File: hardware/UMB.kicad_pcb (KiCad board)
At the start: 6 copper layers, 128.8 x 67 mm, 172 parts, among them J1 PinHeader 02x04, J10 PH1-03-UA, J11 PH1-03-UA, J12 PH1-03-UA, J13 Conn_01x05, J14 Conn_01x05, J15 Conn_01x05, J16 Conn_01x05, J17 Conn_01x05, J18 Conn_01x05, J19 Conn_01x03, J2 PinHeader 02x04, J20 Conn_01x03, J21 Conn_01x03, J22 Conn_01x03, J23 Conn_01x03, J24 Conn_01x03, J25 Conn_01x02, J26 Conn_01x02, J27 FTSH-107-01-L-D-K, J3 PinHeader 02x04, J4 PinHeader 02x04, J5 PinHeader 02x04, J6 PinHeader 02x04, J7 PH1-03-UA, J8 PH1-03-UA, J9 PH1-03-UA, U1 STM32G0C1KCTxN, U10 LDK320ADU120R, U11 INA2128UA_1K, U12 INA2128UA_1K, U13 INA2128UA_1K, U14 TLC274AIDR, U15 TLC274AIDR, U16 TLC274AIDR, U2 ADS114S08BIPBSR, U3 ADM3057ExRW, U4 TPS563300DRLR, U5 TPS563219ADDFR, U6 LM2940SX-12_NOPB, U7 LM1117IMP-5.0, U8 TLV743P, U9 AP2127N3-1.5

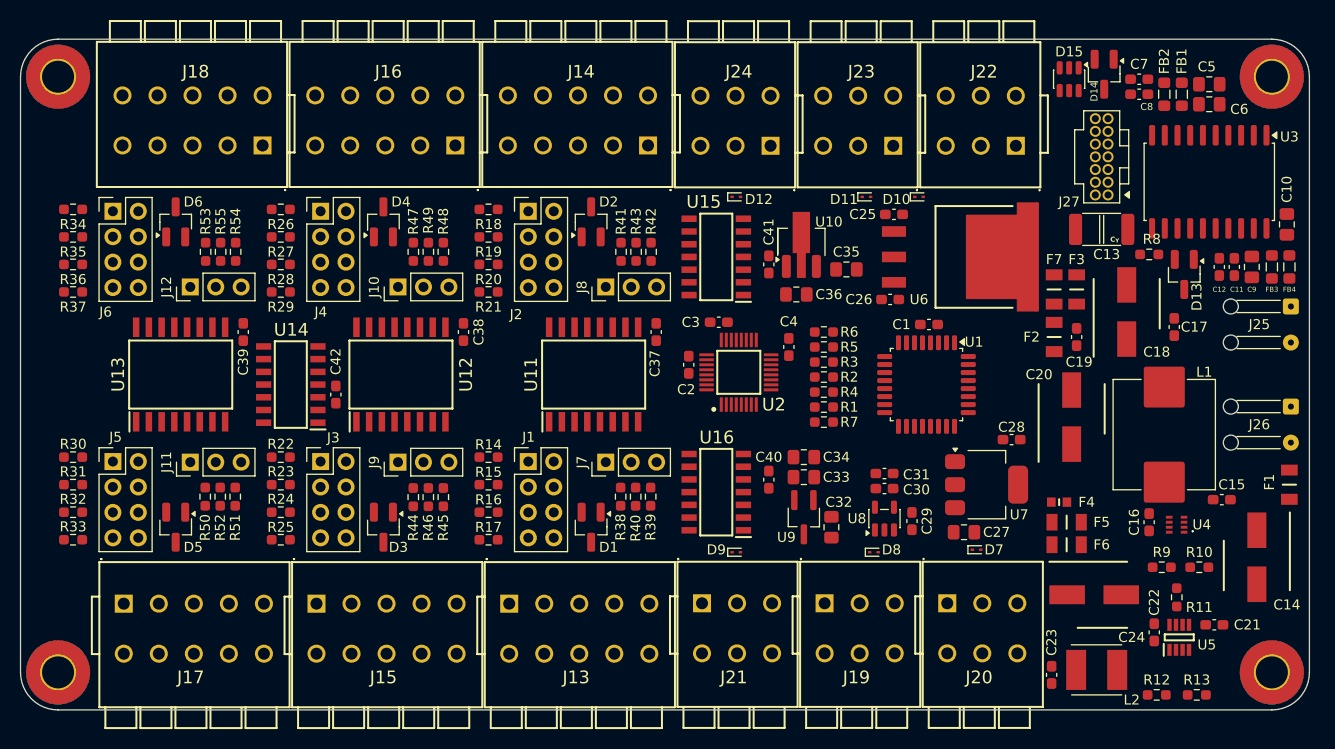
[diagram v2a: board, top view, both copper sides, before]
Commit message: Finished routing on PCB
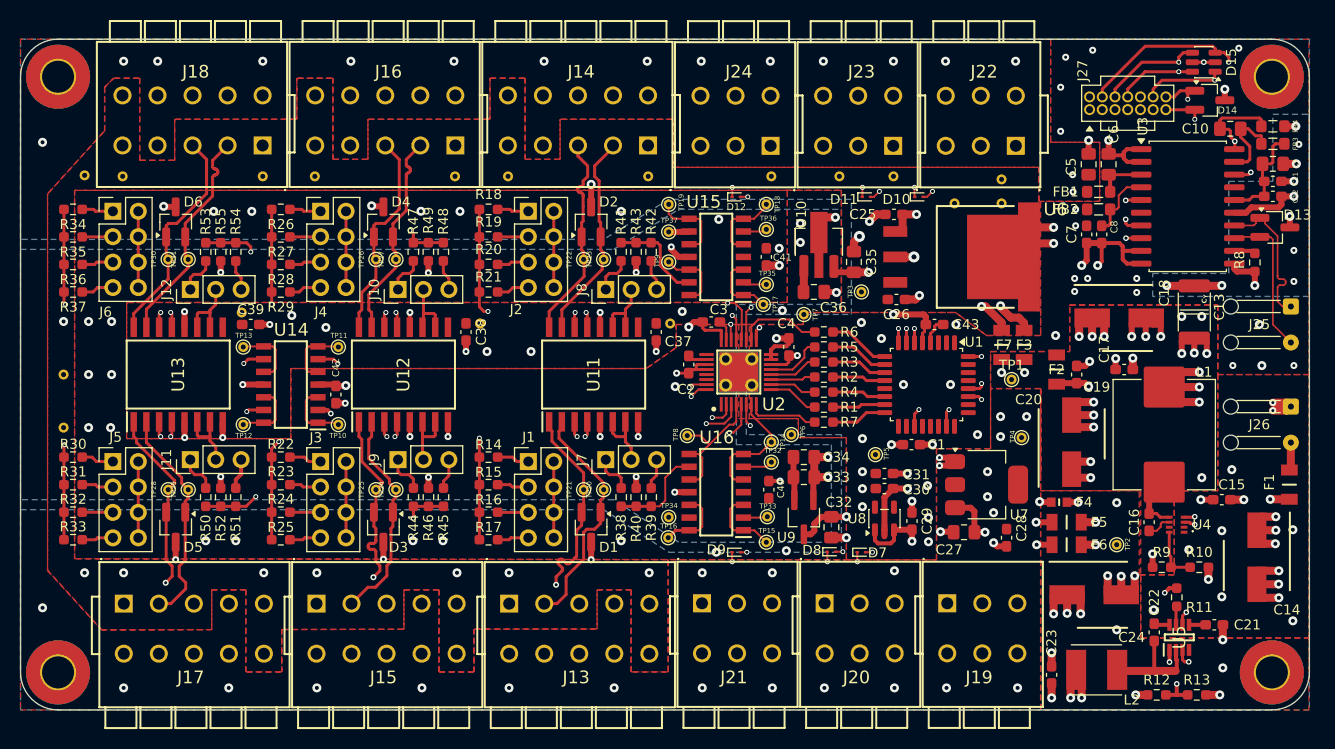
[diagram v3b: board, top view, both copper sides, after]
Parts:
- added ?: , , F.Cu at (74.1, 106.3)
- added ?: , , F.Cu at (150.0, 95.4)
- added ?: , , F.Cu at (56.3, 112.5)
- added ?: , , F.Cu at (114.7, 92.7)
- added ?: , , F.Cu at (133.8, 92.7)
- added ?: , , F.Cu at (145.3, 95.4)
- added ?: , , F.Cu at (127.0, 92.7)
- added ?: , , F.Cu at (100.7, 92.7)
- added ?: , , F.Cu at (139.2, 92.7)
- added ?: , , F.Cu at (150.0, 93.0)
- added ?: , , F.Cu at (62.2, 92.7)
- added ?: , , F.Cu at (95.4, 92.7)
- added ?: , , F.Cu at (58.4, 92.6)
- added ?: , , F.Cu at (76.2, 92.7)
- added ?: , , F.Cu at (56.3, 117.8)
- added ?: , , F.Cu at (97.9, 107.4)
- added ?: , , F.Cu at (81.4, 92.7)
- added ?: , , F.Cu at (116.9, 107.4)
- added C43: 100n, Capacitor_SMD:C_0603_1608Metric_Pad1.08x0.95mm_HandSolder, F.Cu at (143.3, 107.5)
- added NT1: NetTie, NetTie:NetTie-4_THT_Pad1.0mm, B.Cu at (125.0, 111.0)
- added TP1: TestPoint_Small, TestPoint:TestPoint_THTPad_D1.0mm_Drill0.5mm, F.Cu at (151.0, 113.0)
- added TP10: TestPoint_Small, TestPoint:TestPoint_THTPad_D1.0mm_Drill0.5mm, F.Cu at (83.8, 117.5)
- added TP11: TestPoint_Small, TestPoint:TestPoint_THTPad_D1.0mm_Drill0.5mm, F.Cu at (83.8, 109.8)
- added TP12: TestPoint_Small, TestPoint:TestPoint_THTPad_D1.0mm_Drill0.5mm, F.Cu at (74.2, 117.5)
- added TP13: TestPoint_Small, TestPoint:TestPoint_THTPad_D1.0mm_Drill0.5mm, F.Cu at (74.2, 109.8)
- added TP14: TestPoint_Small, TestPoint:TestPoint_THTPad_D1.0mm_Drill0.5mm, F.Cu at (127.0, 119.2)
- added TP15: TestPoint_Small, TestPoint:TestPoint_THTPad_D1.0mm_Drill0.5mm, F.Cu at (126.5, 129.2)
- added TP16: TestPoint_Small, TestPoint:TestPoint_THTPad_D1.0mm_Drill0.5mm, F.Cu at (116.7, 128.8)
- added TP17: TestPoint_Small, TestPoint:TestPoint_THTPad_D1.0mm_Drill0.5mm, F.Cu at (126.2, 105.5)
- added TP18: TestPoint_Small, TestPoint:TestPoint_THTPad_D1.0mm_Drill0.5mm, F.Cu at (126.5, 95.5)
- added TP19: TestPoint_Small, TestPoint:TestPoint_THTPad_D1.0mm_Drill0.5mm, F.Cu at (116.8, 95.5)
- added TP2: TestPoint_Small, TestPoint:TestPoint_THTPad_D1.0mm_Drill0.5mm, F.Cu at (161.5, 129.5)
- added TP20: TestPoint_Small, TestPoint:TestPoint_THTPad_D1.0mm_Drill0.5mm, F.Cu at (110.2, 124.0)
- added TP21: TestPoint_Small, TestPoint:TestPoint_THTPad_D1.0mm_Drill0.5mm, F.Cu at (108.2, 124.0)
- added TP22: TestPoint_Small, TestPoint:TestPoint_THTPad_D1.0mm_Drill0.5mm, F.Cu at (108.2, 101.0)
- added TP23: TestPoint_Small, TestPoint:TestPoint_THTPad_D1.0mm_Drill0.5mm, F.Cu at (110.2, 101.0)
- added TP24: TestPoint_Small, TestPoint:TestPoint_THTPad_D1.0mm_Drill0.5mm, F.Cu at (89.5, 124.0)
- added TP25: TestPoint_Small, TestPoint:TestPoint_THTPad_D1.0mm_Drill0.5mm, F.Cu at (87.5, 124.0)
- added TP26: TestPoint_Small, TestPoint:TestPoint_THTPad_D1.0mm_Drill0.5mm, F.Cu at (87.5, 101.0)
- added TP27: TestPoint_Small, TestPoint:TestPoint_THTPad_D1.0mm_Drill0.5mm, F.Cu at (89.5, 101.0)
- added TP28: TestPoint_Small, TestPoint:TestPoint_THTPad_D1.0mm_Drill0.5mm, F.Cu at (66.8, 124.0)
- added TP29: TestPoint_Small, TestPoint:TestPoint_THTPad_D1.0mm_Drill0.5mm, F.Cu at (68.8, 124.0)
- added TP3: TestPoint_Small, TestPoint:TestPoint_THTPad_D1.0mm_Drill0.5mm, F.Cu at (136.0, 104.2)
- added TP30: TestPoint_Small, TestPoint:TestPoint_THTPad_D1.0mm_Drill0.5mm, F.Cu at (66.8, 101.0)
- added TP31: TestPoint_Small, TestPoint:TestPoint_THTPad_D1.0mm_Drill0.5mm, F.Cu at (68.8, 101.0)
- added TP32: TestPoint_Small, TestPoint:TestPoint_THTPad_D1.0mm_Drill0.5mm, F.Cu at (127.0, 121.2)
- added TP33: TestPoint_Small, TestPoint:TestPoint_THTPad_D1.0mm_Drill0.5mm, F.Cu at (126.6, 126.7)
- added TP34: TestPoint_Small, TestPoint:TestPoint_THTPad_D1.0mm_Drill0.5mm, F.Cu at (116.8, 126.8)
- added TP35: TestPoint_Small, TestPoint:TestPoint_THTPad_D1.0mm_Drill0.5mm, F.Cu at (126.5, 103.5)
- added TP36: TestPoint_Small, TestPoint:TestPoint_THTPad_D1.0mm_Drill0.5mm, F.Cu at (126.5, 98.0)
- added TP37: TestPoint_Small, TestPoint:TestPoint_THTPad_D1.0mm_Drill0.5mm, F.Cu at (116.8, 98.2)
- added TP4: TestPoint_Small, TestPoint:TestPoint_THTPad_D1.0mm_Drill0.5mm, F.Cu at (152.0, 118.8)
- added TP5: TestPoint_Small, TestPoint:TestPoint_THTPad_D1.0mm_Drill0.5mm, F.Cu at (137.4, 120.5)
- added TP6: TestPoint_Small, TestPoint:TestPoint_THTPad_D1.0mm_Drill0.5mm, F.Cu at (129.0, 118.5)
- added TP7: TestPoint_Small, TestPoint:TestPoint_THTPad_D1.0mm_Drill0.5mm, F.Cu at (130.2, 106.5)
- added TP8: TestPoint_Small, TestPoint:TestPoint_THTPad_D1.0mm_Drill0.5mm, F.Cu at (118.6, 118.6)
- added TP9: TestPoint_Small, TestPoint:TestPoint_THTPad_D1.0mm_Drill0.5mm, F.Cu at (116.8, 101.2)
- moved C7 16.4 mm to (158.5, 98.5), turned to -90 degrees
- moved C8 14.5 mm to (160.0, 98.5), turned to -90 degrees
- moved C5 14.5 mm to (158.7, 91.5), turned to -90 degrees
- moved FB4 14.1 mm to (177.1, 87.7), turned to 180 degrees
- moved D15 13.6 mm to (170.2, 81.3), turned to 180 degrees
- moved FB2 13.2 mm to (159.7, 96.0), turned to 180 degrees
- moved FB1 12.8 mm to (159.7, 94.2), turned to 180 degrees
- moved C13 12.4 mm to (169.2, 106.2), turned to 90 degrees
- moved FB3 12.3 mm to (177.1, 89.5), turned to 180 degrees
- moved J19 12.2 mm to (147.8, 139.5)
- moved J20 12.2 mm to (135.5, 139.5)
- moved C1 12.1 mm to (141.0, 119.5)
- moved C6 11.7 mm to (160.7, 91.5), turned to -90 degrees
- moved D7 11.5 mm to (136.0, 130.2)
- moved C10 11.1 mm to (172.8, 88.0), turned to 0 degrees
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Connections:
- D1 pad 1: /Analog/DIF1- -> /Analog/DIF1+
- D1 pad 2: /Analog/DIF1+ -> /Analog/DIF1-
- D14 pad 1: /Connectors/UART_RX -> /Connectors/UART_TX
- D14 pad 2: /Connectors/UART_TX -> /Connectors/UART_RX
- D15 pad 3: /Connectors/SWO -> /Connectors/SWDIO
- D15 pad 6: /Connectors/SWDIO -> /Connectors/SWO
- D2 pad 1: /Analog/DIF2+ -> /Analog/DIF2-
- D2 pad 2: /Analog/DIF2- -> /Analog/DIF2+
- D3 pad 1: /Analog/DIF3- -> /Analog/DIF3+
- D3 pad 2: /Analog/DIF3+ -> /Analog/DIF3-
- D4 pad 1: /Analog/DIF4+ -> /Analog/DIF4-
- D4 pad 2: /Analog/DIF4- -> /Analog/DIF4+
- D5 pad 1: /Analog/DIF5- -> /Analog/DIF5+
- D5 pad 2: /Analog/DIF5+ -> /Analog/DIF5-
- D6 pad 1: /Analog/DIF6+ -> /Analog/DIF6-
- D6 pad 2: /Analog/DIF6- -> /Analog/DIF6+
- J13 pad 2: /Analog/DIF1- -> /Analog/DIF1+
- J13 pad 3: /Analog/DIF1+ -> /Analog/DIF1-
- J14 pad 2: /Analog/DIF2- -> /Analog/DIF2+
- J14 pad 3: /Analog/DIF2+ -> /Analog/DIF2-
- J15 pad 2: /Analog/DIF3- -> /Analog/DIF3+
- J15 pad 3: /Analog/DIF3+ -> /Analog/DIF3-
- J16 pad 2: /Analog/DIF4- -> /Analog/DIF4+
- J16 pad 3: /Analog/DIF4+ -> /Analog/DIF4-
- J17 pad 2: /Analog/DIF5- -> /Analog/DIF5+
- J17 pad 3: /Analog/DIF5+ -> /Analog/DIF5-
- J18 pad 2: /Analog/DIF6- -> /Analog/DIF6+
- J18 pad 3: /Analog/DIF6+ -> /Analog/DIF6-
- R1 pad 1: Net-(U1-PA4) -> Net-(U1-PB0)
- R3 pad 1: Net-(U1-PA6) -> Net-(U1-PA4)
- R5 pad 1: Net-(U1-PB0) -> Net-(U1-PA3)
- R6 pad 1: Net-(U1-PB1) -> Net-(U1-PA2)
- R7 pad 1: Net-(U1-PB6) -> Net-(U1-PB1)
- U1 pad 10: unconnected-(U1-PA3-Pad10) -> Net-(U1-PA3)
- U1 pad 13: Net-(U1-PA6) -> unconnected-(U1-PA6-Pad13)
- U1 pad 24: /Connectors/SWDIO -> unconnected-(U1-PA13-Pad24)
- U1 pad 25: /Connectors/SWCLK -> unconnected-(U1-PA14-Pad25)
- U1 pad 26: /CAN/CAN_RX -> unconnected-(U1-PD0-Pad26)
- U1 pad 30: Net-(U1-PB6) -> unconnected-(U1-PB6-Pad30)
- U1 pad 32: unconnected-(U1-PB8-Pad32) -> /CAN/CAN_RX
- U1 pad 7: unconnected-(U1-PA0-Pad7) -> /Connectors/SWCLK
- U1 pad 8: unconnected-(U1-PA1-Pad8) -> /Connectors/SWDIO
- U1 pad 9: unconnected-(U1-PA2-Pad9) -> Net-(U1-PA2)
- U12 pad 1: /Analog/DIF3+ -> /Analog/DIF3-
- U12 pad 2: /Analog/DIF3- -> /Analog/DIF3+
- U2 pad 19: /ADC/DIF6 -> /ADC/SE4
- U2 pad 2: /ADC/SE6 -> /ADC/DIF3
- U2 pad 20: /ADC/DIF5 -> /ADC/SE5
- U2 pad 21: /ADC/DIF4 -> /ADC/DIF2
- U2 pad 22: /ADC/DIF3 -> /ADC/SE6
- U2 pad 3: /ADC/SE5 -> /ADC/DIF5
- U2 pad 31: /ADC/DIF2 -> /ADC/DIF6
- U2 pad 32: /ADC/DIF1 -> /ADC/DIF4
- U2 pad 4: /ADC/SE4 -> /ADC/DIF1
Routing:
- net GND: track 0.00 -> 149.1 mm, vias 0 -> 62
- net /Connectors/SWDIO: track 0.00 -> 121.0 mm, vias 0 -> 2
- net /ADC/DIF6: track 0.00 -> 62.8 mm, vias 0 -> 1
- net /Connectors/SWCLK: track 0.00 -> 60.8 mm, vias 0 -> 2
- net /Connectors/NRST: track 0.00 -> 60.3 mm, vias 0 -> 2
- net /ADC/DIF5: track 0.00 -> 58.9 mm, vias 0 -> 1
- net AGND: track 0.00 -> 57.8 mm, vias 0 -> 30
- net /ADC/DIF4: track 0.00 -> 55.6 mm, vias 0 -> 1
- net /Connectors/UART_TX: track 0.00 -> 53.2 mm, vias 0 -> 2
- net Net-(U5-VIN): track 0.00 -> 49.3 mm, vias 0 -> 5
- net /ADC/DIF3: track 0.00 -> 48.9 mm, vias 0 -> 1
- net /Connectors/UART_RX: track 0.00 -> 48.7 mm, vias 0 -> 2
- net SE4IN: track 0.00 -> 40.4 mm, vias 0 -> 1
- net SE1IN: track 0.00 -> 38.8 mm, vias 0 -> 1
- net /CAN/CAN_STBY: track 0.00 -> 31.6 mm, vias 0 -> 2
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- added copper zone on F.Cu, net +12V
- added copper zone on In2.Cu, net +12V
- added copper zone on In4.Cu, net +12V
- added copper zone on F.Cu, net +12VA
- added copper zone on In2.Cu, net +12VA
- added copper zone on In4.Cu, net +12VA
- added copper zone on F.Cu, net +14.5V
- added copper zone on In2.Cu, net +14.5V
- added copper zone on In4.Cu, net +14.5V
- added copper zone on F.Cu, net +3.3V
- added copper zone on In2.Cu, net +3.3V
- added copper zone on In4.Cu, net +3.3V
- added copper zone on F.Cu, net +5V
- added copper zone on In2.Cu, net +5V
- added copper zone on In4.Cu, net +5V
- added copper zone on F.Cu, net +5VA
- added copper zone on In2.Cu, net +5VA
- added copper zone on In4.Cu, net +5VA
- added copper zone on F.Cu, net +7V
- added copper zone on In2.Cu, net +7V
- added copper zone on In4.Cu, net +7V
- added copper zone on B.Cu, net /CAN/GND_CAN_ISO
- added copper zone on In1.Cu, net /CAN/GND_CAN_ISO
- added copper zone on In3.Cu, net /CAN/GND_CAN_ISO
- added copper zone on B.Cu, net AGND
- added copper zone on In1.Cu, net AGND
- added copper zone on In3.Cu, net AGND
- added copper zone on B.Cu, net GND
- added copper zone on In1.Cu, net GND
- added copper zone on In3.Cu, net GND
- added copper zone on F.Cu, net Net-(U4-VIN)
- added copper zone on In2.Cu, net Net-(U4-VIN)
- added copper zone on In4.Cu, net Net-(U4-VIN)

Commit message: Corrections after review
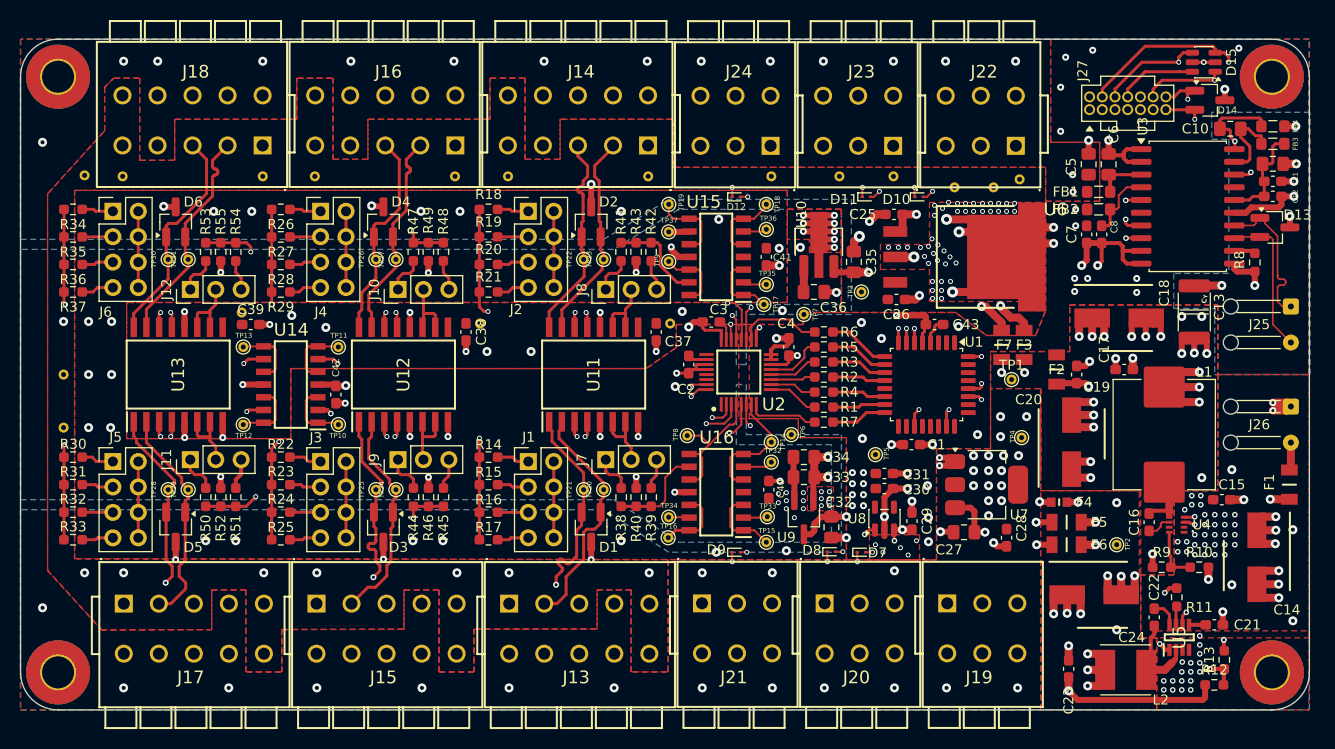
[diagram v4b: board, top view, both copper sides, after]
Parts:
- removed NT1: NetTie, NetTie:NetTie-4_THT_Pad1.0mm
- moved R12 5.84 mm to (171.2, 143.5)
- moved R13 4.45 mm to (172.2, 141.0), turned to 90 degrees
- moved L2 2.90 mm to (162.4, 142.0)
- moved C23 1.80 mm to (156.7, 141.9), turned to 90 degrees
- moved ? 1.80 mm to (151.8, 93.0)
- moved ? 1.79 mm to (149.2, 93.8)
- moved ? 1.60 mm to (145.3, 93.8)
- moved C22 1.50 mm to (165.2, 136.8)
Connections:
- C2 pad 2: AGND -> GND
- C3 pad 1: AGND -> GND
- C33 pad 2: AGND -> GND
- C34 pad 2: AGND -> GND
- C36 pad 2: AGND -> GND
- C37 pad 1: AGND -> GND
- C38 pad 1: AGND -> GND
- C39 pad 1: AGND -> GND
- C40 pad 2: AGND -> GND
- C41 pad 2: AGND -> GND
- C42 pad 2: AGND -> GND
- R40 pad 2: AGND -> GND
- R43 pad 2: AGND -> GND
- R46 pad 2: AGND -> GND
- R49 pad 2: AGND -> GND
- R52 pad 2: AGND -> GND
- R55 pad 2: AGND -> GND
- U10 pad 2: AGND -> GND
- U11 pad 12: AGND -> GND
- U11 pad 5: AGND -> GND
- U11 pad 8: AGND -> GND
- U12 pad 12: AGND -> GND
- U12 pad 5: AGND -> GND
- U12 pad 8: AGND -> GND
- U13 pad 12: AGND -> GND
- U13 pad 5: AGND -> GND
- U13 pad 8: AGND -> GND
- U14 pad 11: AGND -> GND
- U15 pad 11: AGND -> GND
- U16 pad 11: AGND -> GND
- U2 pad 24: AGND -> GND
- U2 pad 27: AGND -> GND
- U2 pad 28: AGND -> GND
- U9 pad 1: AGND -> GND
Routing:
- net GND: track 149.1 -> 212.4 mm, vias 62 -> 157
- net AGND: track 57.8 -> 0.00 mm, vias 30 -> 0
- net /Connectors/SWDIO: track 121.0 -> 73.4 mm
- net +7V: track 20.9 -> 36.9 mm, vias 13 -> 12
- net Net-(U5-SW): track 16.8 -> 7.45 mm
- net Net-(U5-VFB): track 14.5 -> 10.9 mm
- net Net-(U8-EN): track 23.7 -> 26.8 mm, vias 2 -> 4
- net /CAN/GND_CAN_ISO: track 21.5 -> 18.8 mm, vias 8 -> 7
- net +14.5V: track 24.1 -> 21.8 mm, vias 13 -> 12
- net /ADC/SE5: track 27.1 -> 25.0 mm
- net SE3IN: track 19.5 -> 21.5 mm
- net Net-(U4-VIN): track 12.1 -> 10.9 mm, vias 13 -> 40
- net Net-(U5-VBST): track 1.57 -> 2.79 mm
- net Net-(U5-VIN): track 49.3 -> 48.2 mm, vias 5 -> 21
- net Net-(U4-SW): track 5.92 -> 5.36 mm
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- added copper zone on F.Cu, net GND
- added copper zone on F.Cu, net Net-(U5-VIN)
- added copper zone on In2.Cu, net Net-(U5-VIN)
- added copper zone on In4.Cu, net Net-(U5-VIN)
- removed copper zone on B.Cu, net AGND
- removed copper zone on In1.Cu, net AGND
- removed copper zone on In3.Cu, net AGND
